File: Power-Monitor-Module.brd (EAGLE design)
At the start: 20.3 x 12.7 mm, 17 parts, among them IC1 INA231, P1 2X5P, P2 2X5P, P3 1X4P

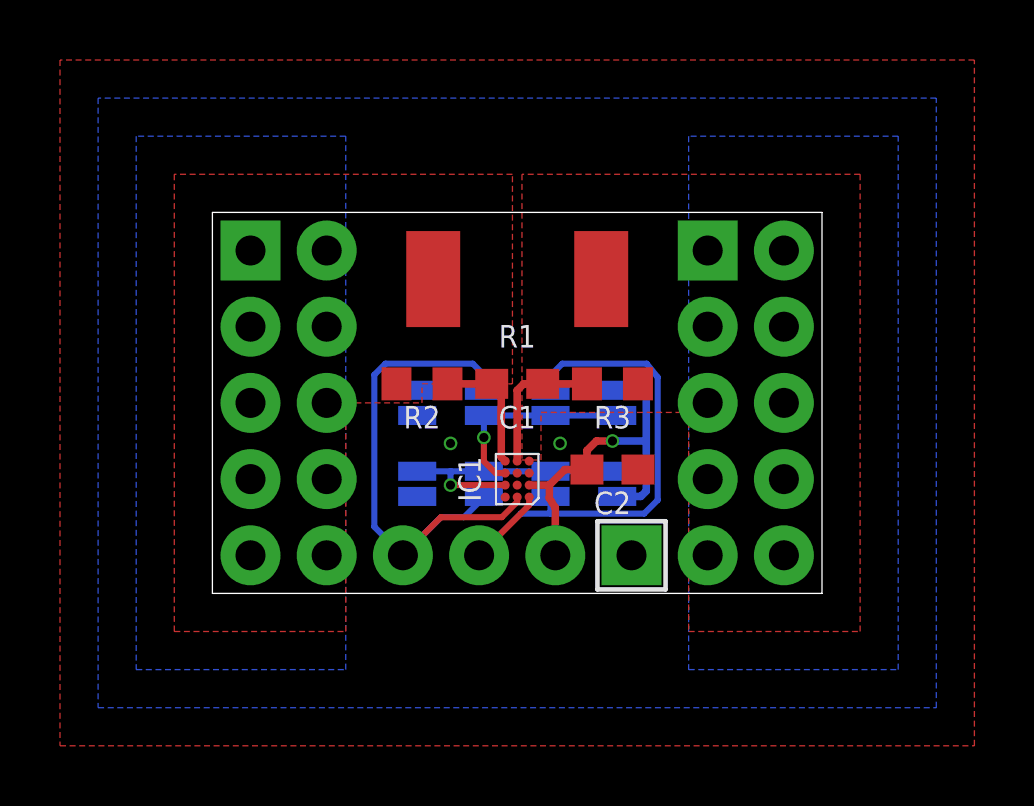
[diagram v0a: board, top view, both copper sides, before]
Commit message: Made Rev.2 with the measurement IC changed to INA226.
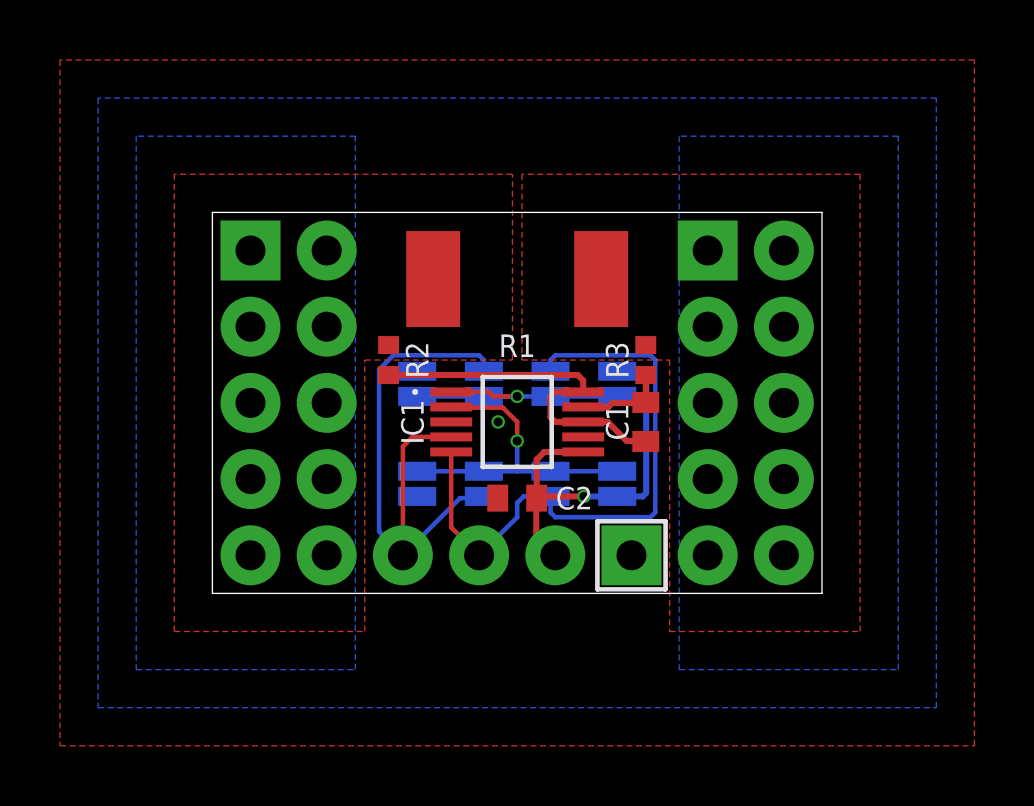
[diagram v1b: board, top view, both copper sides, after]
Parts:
- C1, C2: device rcl:C0603 -> rcl:C0402
- IC1: value INA231 -> INA226; device INA231:INA231 -> INA226:MSOP-10
- R2, R3: value 10 -> 4.7; device rcl:R0603 -> rcl:R0402
- moved C1 4.47 mm to (4.29, -0.64), turned to 90 degrees
- moved C2 3.31 mm to (0.00, -3.17), turned to 180 degrees
- moved IC1 1.91 mm to (0.00, -0.64), turned to 0 degrees
- moved R2 1.37 mm to (-4.29, 1.43), turned to 270 degrees
- moved R3 1.37 mm to (4.29, 1.43), turned to 270 degrees
- moved JP5 0.64 mm to (-3.33, 0.64)
- moved JP6 0.64 mm to (3.33, 0.64)
- moved JP7 0.64 mm to (-1.11, 0.64)
- moved JP8 0.64 mm to (1.11, 0.64)
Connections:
- net A0: now also IC1.2; no longer IC1.B3
- net A1: now also IC1.1; no longer IC1.C3
- net ALERT: now also IC1.3; no longer IC1.A3
- net GND: now also IC1.7; no longer IC1.C1
- net IN+: now also IC1.10, IC1.8; no longer IC1.D3
- net IN-: now also IC1.9; no longer IC1.D2
- net SCL: now also IC1.5; no longer IC1.A1
- net SDA: now also IC1.4; no longer IC1.A2
- net VIN-: no longer IC1.D1
- net VS: now also IC1.6; no longer IC1.B1
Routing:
- net IN+: track 4.24 -> 12.3 mm
- net A1: track 6.85 -> 9.03 mm
- net SCL: track 18.7 -> 20.5 mm
- net IN-: track 4.77 -> 3.09 mm
- net A0: track 9.25 -> 10.8 mm
- net VS: track 12.5 -> 13.9 mm
- net SDA: track 19.1 -> 19.8 mm
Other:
- board text added: "Power Monitor Module Rev. 2 Designed by Masato Kubotera on May 4, 2023."
- board text removed: "Power Monitor Module Rev. 1 Designed by Masato Kubotera on April 22, 2023."
